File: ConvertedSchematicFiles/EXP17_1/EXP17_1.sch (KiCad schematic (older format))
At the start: 9 parts

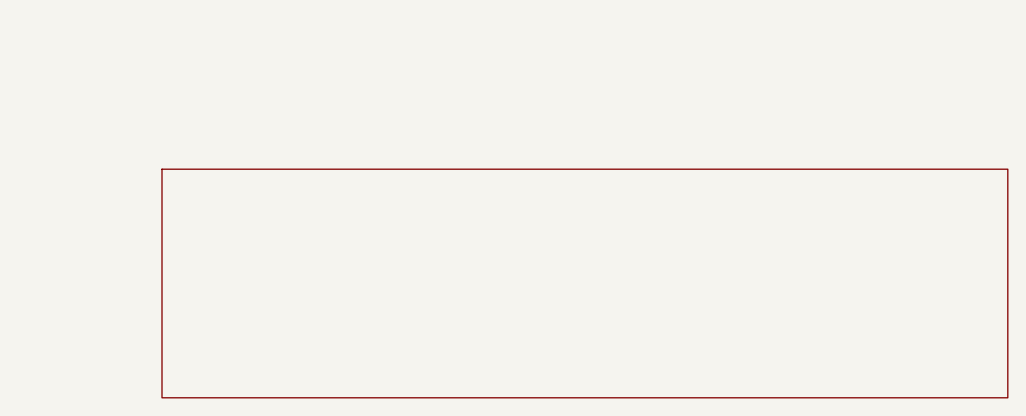
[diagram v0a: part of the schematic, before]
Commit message: Excluded some components. These no longer appear after conversion. When calling shell commands, filenames are in "quotes"
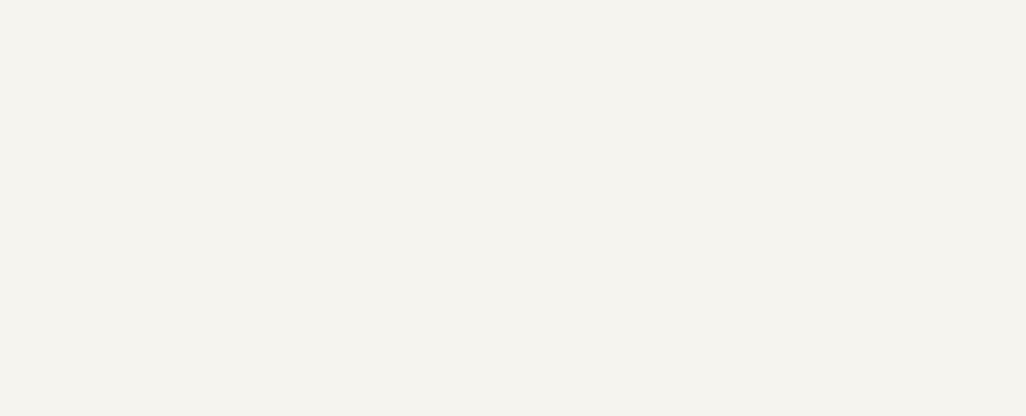
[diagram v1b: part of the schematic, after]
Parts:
- removed titleblk: titleblk, symbol TITLEBLK_PSPICE
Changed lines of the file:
@@
-	1    0    0    1
-$EndComp
-$Comp
-L TITLEBLK_PSPICE titleblk
-U 1 1 66516649
-P 9700 7200
-F 0 "titleblk" H 19400 14400 30  0001 L CNN
-F 1 "titleblk" H 19400 14480 30  0001 L CNN
-	1    9700 7200
 	1    0    0    1
 $EndComp

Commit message: Ports issue fixed. Now annotation for ports is #PWR? function added "itos"
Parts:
- removed EGND (x2): EGND, symbol EGND_PSPICE
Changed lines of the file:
@@
 $EndDescr
 $Comp
-L EGND_PSPICE EGND
+L EGND_PSPICE #PWR1
 U 1 1 14289383
 P 1600 1100
-F 0 "EGND" H 3200 2200 30  0001 L CNN
+F 0 "#PWR1" H 3200 2200 30  0001 L CNN
 F 1 "EGND" H 3200 2280 30  0001 L CNN
 	1    1600 1100
@@
 $EndComp
 $Comp
-L EGND_PSPICE EGND
+L EGND_PSPICE #PWR2
 U 1 1 46930886
 P 3500 1100
-F 0 "EGND" H 7000 2200 30  0001 L CNN
+F 0 "#PWR2" H 7000 2200 30  0001 L CNN
 F 1 "EGND" H 7000 2280 30  0001 L CNN
 	1    3500 1100

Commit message: Added LICENSE.txt
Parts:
- V1, V2: value VPULSE -> PULSE
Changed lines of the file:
@@
 $EndDescr
 $Comp
-L EGND_PSPICE #PWR1
+L GND #PWR1
 U 1 1 14289383
 P 1600 1100
@@
 $EndComp
 $Comp
-L EGND_PSPICE #PWR2
+L GND #PWR2
 U 1 1 46930886
 P 3500 1100
@@
 P 700 700
 F 0 "V1" H 700 700 30  0001 L CNN
-F 1 "VPULSE" H 700 780 30  0001 L CNN
+F 1 "PULSE" H 700 780 30  0001 L CNN
 	1    700 700
 	1    0    0    1
@@
 P 2600 700
 F 0 "V2" H 2600 700 30  0001 L CNN
-F 1 "VPULSE" H 2600 780 30  0001 L CNN
+F 1 "PULSE" H 2600 780 30  0001 L CNN
 	1    2600 700
 	1    0    0    1

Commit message: Orientation fix. Library components are now inverted, with +ve y axis going up. In Schematic files, +ve y axis is downwards. This is how the KiCad libraries are. As a result of the above fixed, the converted GND is now oriented correctly.
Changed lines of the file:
@@
 F 1 "EGND" H 3200 2280 30  0001 L CNN
 	1    1600 1100
-	1    0    0    1
+	1    0    0    -1
 $EndComp
 $Comp
@@
 F 1 "EGND" H 7000 2280 30  0001 L CNN
 	1    3500 1100
-	1    0    0    1
+	1    0    0    -1
 $EndComp
 $Comp
@@
 F 1 "10k" H 1000 800 30  0000 L CNN
 	1    1000 700
-	1    0    0    1
+	1    0    0    -1
 $EndComp
 $Comp
@@
 F 1 "10u" H 1600 1000 30  0000 L CNN
 	1    1600 700
-	0    -1    1    0
+	0    1    1    0
 $EndComp
 $Comp
@@
 F 1 "10u" H 3500 1000 30  0000 L CNN
 	1    3500 700
-	0    -1    1    0
+	0    1    1    0
 $EndComp
 $Comp
@@
 F 1 "20k" H 2900 800 30  0000 L CNN
 	1    2900 700
-	1    0    0    1
+	1    0    0    -1
 $EndComp
 $Comp
@@
 F 1 "PULSE" H 700 780 30  0001 L CNN
 	1    700 700
-	1    0    0    1
+	1    0    0    -1
 $EndComp
 $Comp
@@
 F 1 "PULSE" H 2600 780 30  0001 L CNN
 	1    2600 700
-	1    0    0    1
+	1    0    0    -1
 $EndComp
 Wire Wire Line

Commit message: Removed the use of exec, wrote basename function, made integration with eSim easier.
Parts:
- added titleblk: titleblk, symbol titleblk_PSPICE
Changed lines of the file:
@@
-EESchema Schematic File Version 2  date Sunday 27 February 2000 02:48:43 PM IST
+EESchema Schematic File Version 2  date
 LIBS:power
 LIBS:device
@@
 LIBS:contrib
 LIBS:valves
-LIBS:ConvertedSchematicFiles/EXP17_1-cache
 EELAYER 25  0
 EELAYER END
@@
 Sheet 1 1
 Title ""
-Date "27 Feb 2000"
+Date ""
 Rev ""
 Comp ""
@@
 	1    0    0    -1
 $EndComp
+$Comp
+L titleblk_PSPICE titleblk
+U 1 1 66516649
+P 9700 7200
+F 0 "titleblk" H 19400 14400 30  0001 L CNN
+F 1 "titleblk" H 19400 14480 30  0001 L CNN
+	1    9700 7200
+	1    0    0    -1
+$EndComp
